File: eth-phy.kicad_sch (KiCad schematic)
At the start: 42 parts, among them U28 RTL8211FDI-CG, Y5 Resonator_25MHz_445

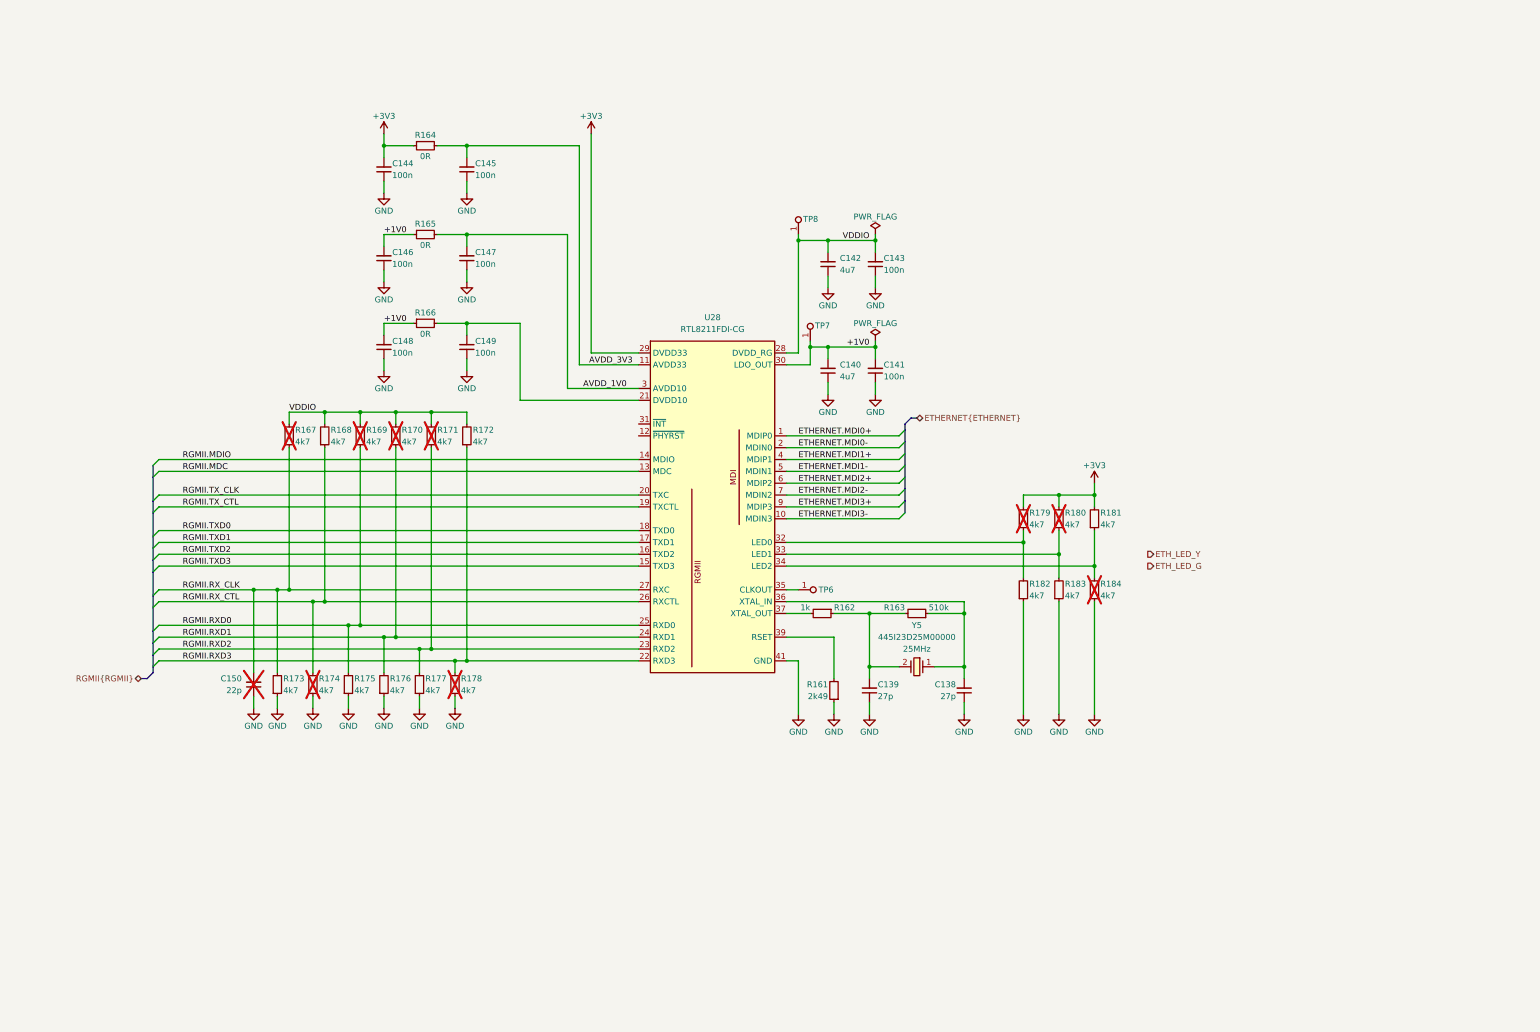
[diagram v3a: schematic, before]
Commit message: [#83329] Finish connecting ETH PHY, connect ETH LEDs, adjust PHY power supply filtering
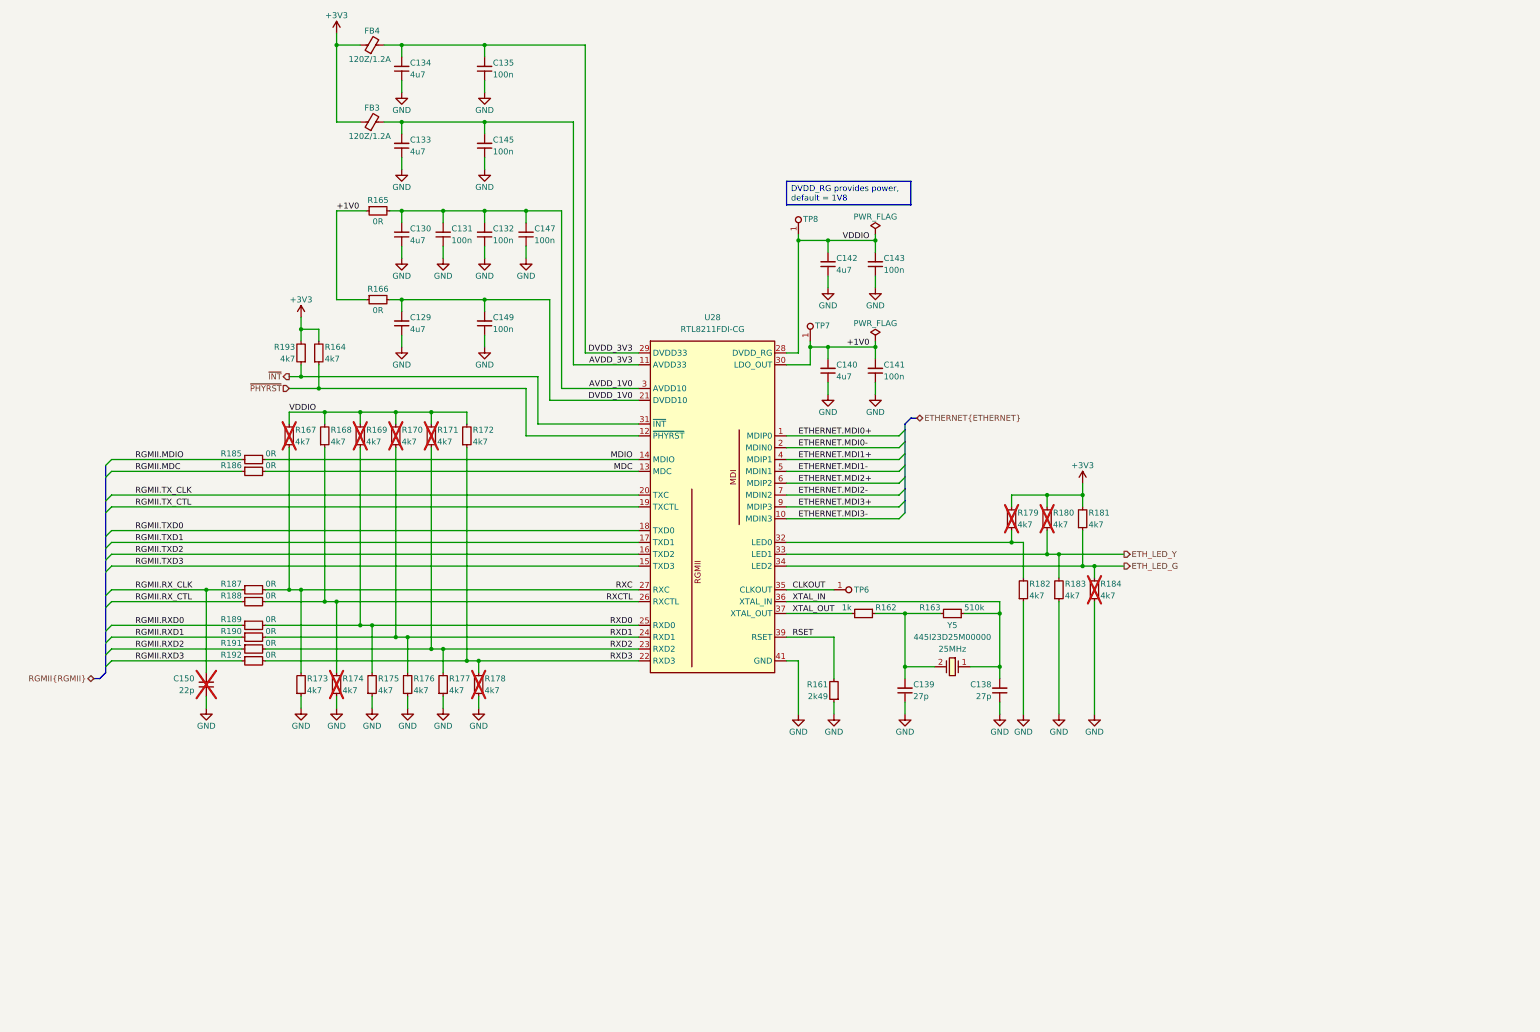
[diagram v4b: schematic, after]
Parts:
- removed C144, C146, C148: C_100n_0402, antmicro-footprints:C_0402_1005Metric, symbol antmicroCapacitors0402:C_100n_0402
- removed R164: R_0R_0402, antmicro-footprints:R_0402_1005Metric, symbol antmicroResistors0402:R_0R_0402
- added C129, C130, C133, C134: C_4u7_0402, antmicro-footprints:C_0402_1005Metric, symbol antmicroCapacitors0402:C_4u7_0402
- added C131, C132, C135: C_100n_0402, antmicro-footprints:C_0402_1005Metric, symbol antmicroCapacitors0402:C_100n_0402
- added FB3, FB4: FB_120Z_1.2A_TDK-MPZ_0402, antmicro-footprints:FB_0402_1005Metric, symbol antmicroFerriteBeadsandChips:FB_120Z_1.2A_TDK-MPZ_0402
- added R164, R193: R_4k7_0402, antmicro-footprints:R_0402_1005Metric, symbol antmicroResistors0402:R_4k7_0402
- added R185, R186, R187, R188, R189, R190, R191, R192: R_0R_0402, antmicro-footprints:R_0402_1005Metric, symbol antmicroResistors0402:R_0R_0402
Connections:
- net +3V3: now also FB3.1, FB4.1, R164.2, R193.2; no longer U28.29 (DVDD33)
- net AVDD_1V0: now also C130.2, C131.2, C132.2
- net AVDD_3V3: now also C133.2, FB3.2
- net ETH_LED_G: now also R181.1, R184.2, U28.34 (LED2)
- net ETH_LED_Y: now also R180.1, R183.2, U28.33 (LED1)
- net GND: now also C129.1, C130.1, C131.1, C132.1, C133.1, C134.1, C135.1
- net RGMII.MDC: now also R186.1; no longer U28.13 (MDC)
- net RGMII.MDIO: now also R185.1; no longer U28.14 (MDIO)
- net RGMII.RXD0: now also R189.1; no longer R169.1, R175.2, U28.25 (RXD0)
- net RGMII.RXD1: now also R190.1; no longer R170.1, R176.2, U28.24 (RXD1)
- net RGMII.RXD2: now also R191.1; no longer R171.1, R177.2, U28.23 (RXD2)
- net RGMII.RXD3: now also R192.1; no longer R172.1, R178.2, U28.22 (RXD3)
- net RGMII.RX_CLK: now also R187.1; no longer R167.1, R173.2, U28.27 (RXC)
- net RGMII.RX_CTL: now also R188.1; no longer R168.1, R174.2, U28.26 (RXCTL)
- net DVDD_1V0: now reaches C149.2, R166.2, U28.21 (DVDD10)
- net DVDD_1V0: now also C129.2
- net XTAL_IN: now reaches C138.2, R163.1, U28.36 (XTAL_IN), Y5.1
- net CLKOUT: now reaches TP6.1, U28.35 (CLKOUT)
- net RSET: now reaches R161.2, U28.39 (RSET)
- net XTAL_OUT: now reaches R162.2, U28.37 (XTAL_OUT)
- net ~{PHYRST}: now reaches U28.12 (~{PHYRST})
- net ~{PHYRST}: now also R164.1
- net ~{INT}: now reaches U28.31 (~{INT})
- net ~{INT}: now also R193.1
- new net DVDD_3V3: C134.2, C135.2, FB4.2, U28.29 (DVDD33)
- new net MDC: R186.2, U28.13 (MDC)
- new net MDIO: R185.2, U28.14 (MDIO)
- new net RXC: R167.1, R173.2, R187.2, U28.27 (RXC)
- new net RXCTL: R168.1, R174.2, R188.2, U28.26 (RXCTL)
- new net RXD0: R169.1, R175.2, R189.2, U28.25 (RXD0)
- new net RXD1: R170.1, R176.2, R190.2, U28.24 (RXD1)
- new net RXD2: R171.1, R177.2, R191.2, U28.23 (RXD2)
- new net RXD3: R172.1, R178.2, R192.2, U28.22 (RXD3)
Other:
- moved on the sheet: C138, C139, C145, C147, C149, C150, R162, R163, R165, R166, R173, R174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

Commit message: [#83329] Add TVS to Ethernet pins
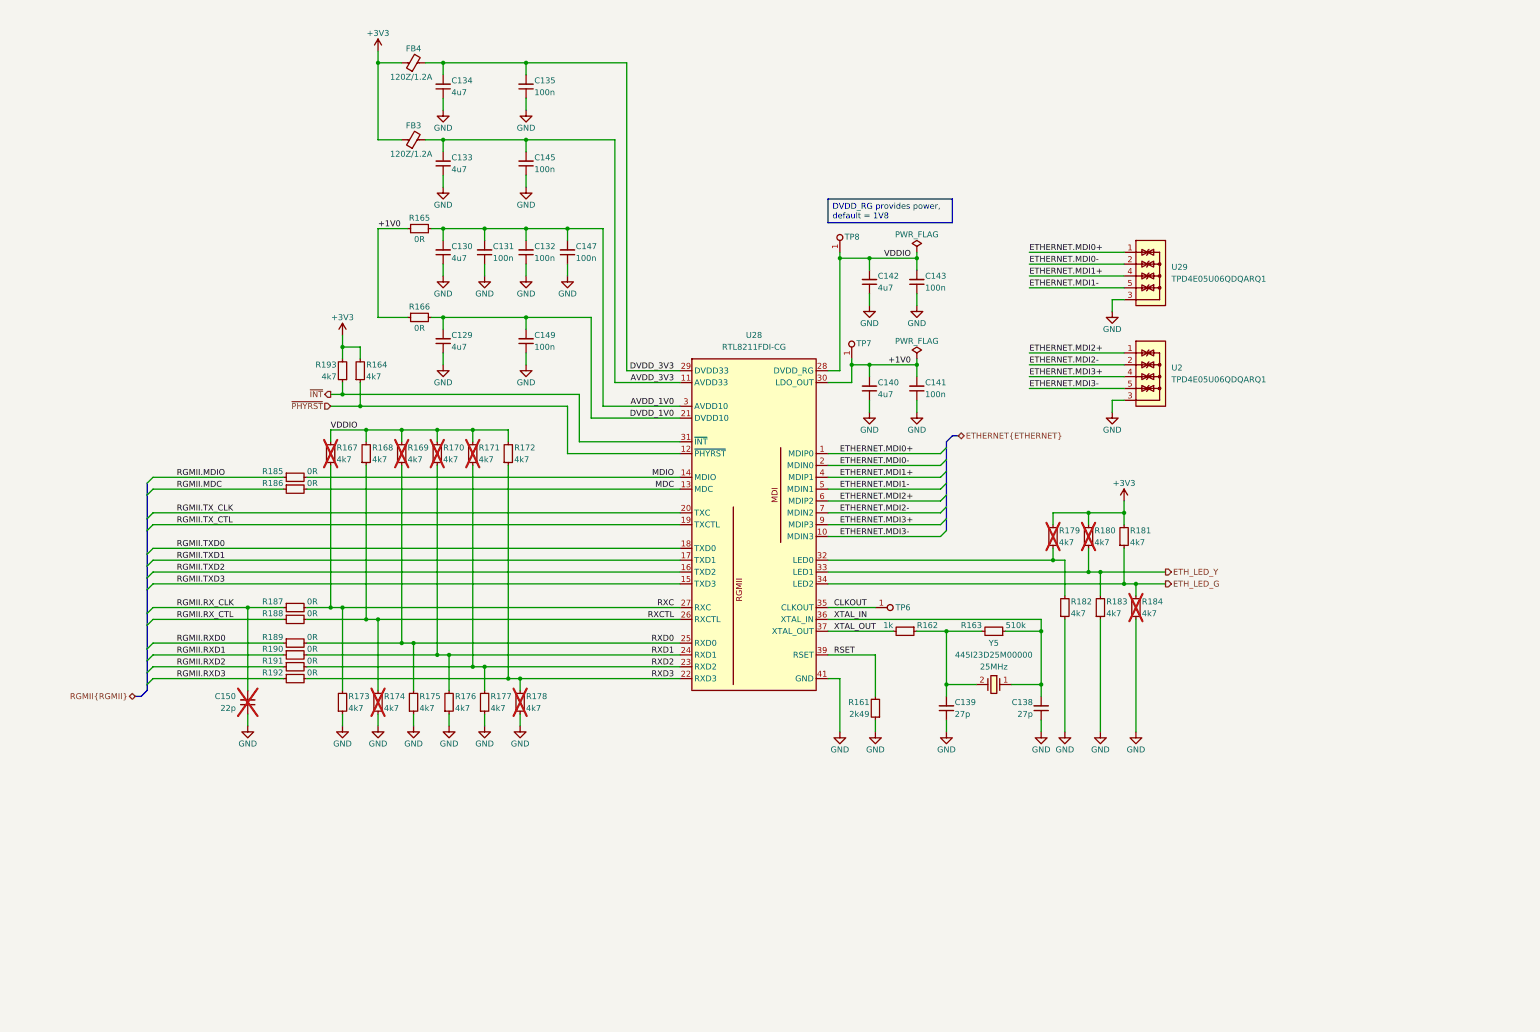
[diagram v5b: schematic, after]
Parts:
- added U2, U29: TPD4E05U06QDQARQ1, antmicro-footprints:USON-10_2.5x1mm_P0.5mm, symbol antmicroTVSDiodes:TPD4E05U06QDQARQ1
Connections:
- net ETHERNET.MDI0+: now also U29.1, U29.10
- net ETHERNET.MDI0-: now also U29.2, U29.9
- net ETHERNET.MDI1+: now also U29.4, U29.7
- net ETHERNET.MDI1-: now also U29.5, U29.6
- net ETHERNET.MDI2+: now also U2.1, U2.10
- net ETHERNET.MDI2-: now also U2.2, U2.9
- net ETHERNET.MDI3+: now also U2.4, U2.7
- net ETHERNET.MDI3-: now also U2.5, U2.6
- net GND: now also U2.3, U2.8, U29.3, U29.8
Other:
- moved on the sheet: C129, C130, C131, C132, C133, C134, C135, C138, C139, C140, C141, C142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

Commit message: [#83329] Update ETH PHY IC footprint
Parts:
- U28: footprint antmicro-footprints:UQFN-40-1EP_5x5mm_P0.4mm_EP3.8x3.8mm -> antmicro-footprints:QFN-40-1EP_5x5mm_P0.4mm_EP3.7x3.7mm
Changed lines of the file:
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@@
 			)
 		)
-		(property "Footprint" "antmicro-footprints:UQFN-40-1EP_5x5mm_P0.4mm_EP3.8x3.8mm"
+		(property "Footprint" "antmicro-footprints:QFN-40-1EP_5x5mm_P0.4mm_EP3.7x3.7mm"
 			(at 240.03 140.97 0)
 			(effects

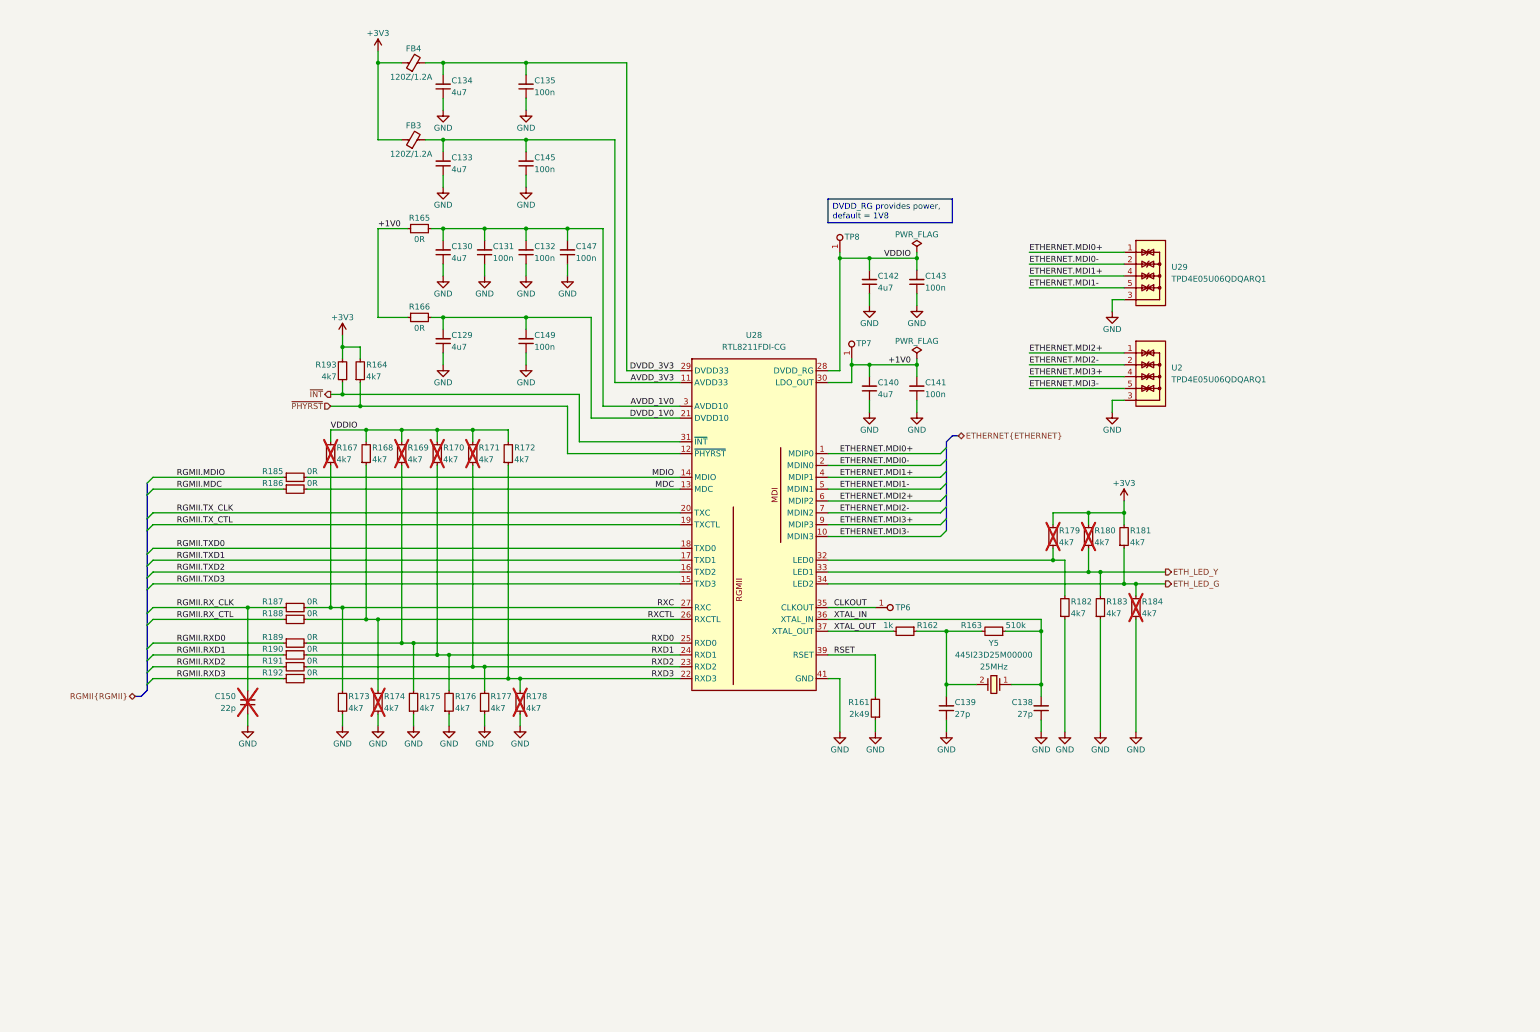
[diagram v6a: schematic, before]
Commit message: [#83329] Small ethernet PHY fixes
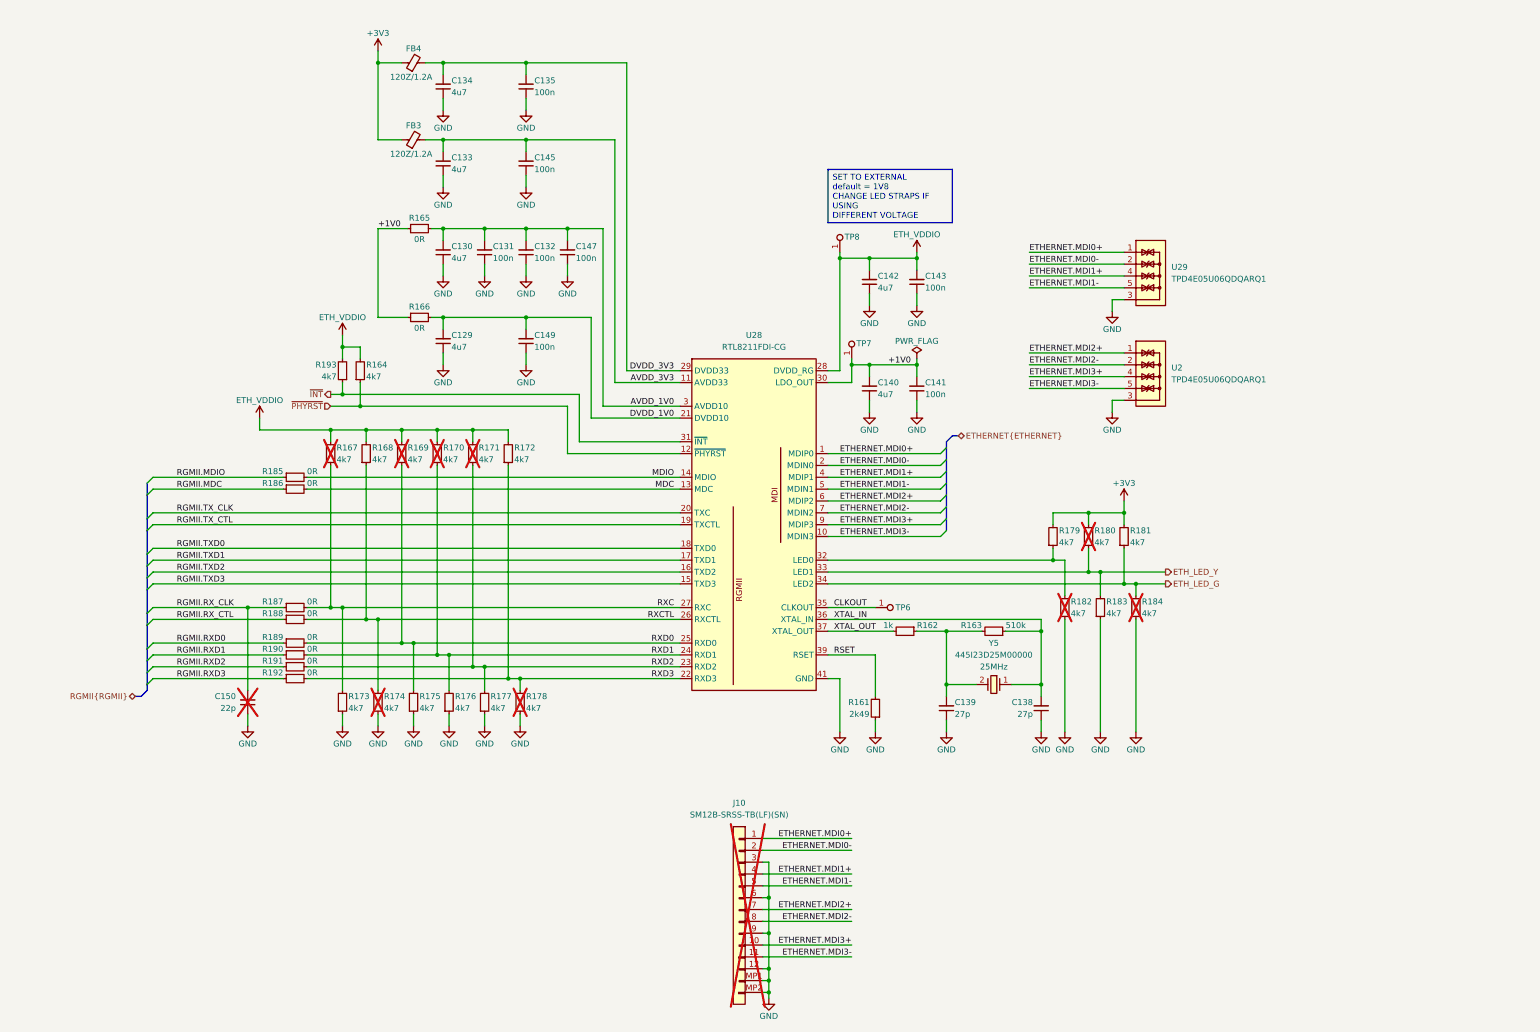
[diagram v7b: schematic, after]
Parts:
- added J10: JST_SH_1x12_SM12B-SRSS-TB-LF-SN, antmicro-footprints:Conn_JST_SH_1x12_SM12B-SRSS-TB-LF-SN, symbol antmicroWire2BoardConnectors:JST_SH_1x12_SM12B-SRSS-TB-LF-SN
- R179: now fitted
- R182: now not fitted
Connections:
- net +3V3: no longer R164.2, R193.2
- net ETHERNET.MDI0+: now also J10.1
- net ETHERNET.MDI0-: now also J10.2
- net ETHERNET.MDI1+: now also J10.4
- net ETHERNET.MDI1-: now also J10.5
- net ETHERNET.MDI2+: now also J10.7
- net ETHERNET.MDI2-: now also J10.8
- net ETHERNET.MDI3+: now also J10.10
- net ETHERNET.MDI3-: now also J10.11
- net GND: now also J10.12, J10.3, J10.6, J10.9, J10.MP1, J10.MP2
- net VDDIO renamed ETH_VDDIO
- net ETH_VDDIO: now also R164.2, R193.2
